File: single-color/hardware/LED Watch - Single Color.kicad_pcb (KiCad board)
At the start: 4 copper layers, 42 x 51.2 mm, 197 parts, among them J1 LiPo, J1B LiPo, J2 UPDI pogo pads 1.27 mm (RESET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, M0 LED white 0402, M1 LED white 0402, M10 LED white 0402, M11 LED white 0402, M12 LED white 0402, M13 LED white 0402, M14 LED white 0402, M15 LED white 0402, M16 LED white 0402, M17 LED white 0402, M18 LED white 0402, M19 LED white 0402, M2 LED white 0402, M20 LED white 0402, M21 LED white 0402, M22 LED white 0402, M23 LED white 0402, M24 LED white 0402, M25 LED white 0402, M26 LED white 0402, M27 LED white 0402, M28 LED white 0402, M29 LED white 0402, M3 LED white 0402, M30 LED white 0402, M31 LED white 0402, M32 LED white 0402, M33 LED white 0402, M34 LED white 0402, M35 LED white 0402, M36 LED white 0402, M37 LED white 0402, M38 LED white 0402, M39 LED white 0402, M4 LED white 0402, M40 LED white 0402, M41 LED white 0402, M42 LED white 0402, M43 LED white 0402, M44 LED white 0402, M45 LED white 0402, M46 LED white 0402, M47 LED white 0402, M48 LED white 0402, M49 LED white 0402, M5 LED white 0402, M50 LED white 0402, M51 LED white 0402, M52 LED white 0402, M53 LED white 0402, M54 LED white 0402, M55 LED white 0402, M56 LED white 0402, M57 LED white 0402, M58 LED white 0402, M59 LED white 0402, M6 LED white 0402, M7 LED white 0402, M8 LED white 0402, M9 LED white 0402, SW1 SW_Push, SW2 SW_Push, U1 AVR128DB48-I/6LX, U2 LIS2DW12TR, U4 BQ25570RGRR, Y1 32.768kHz

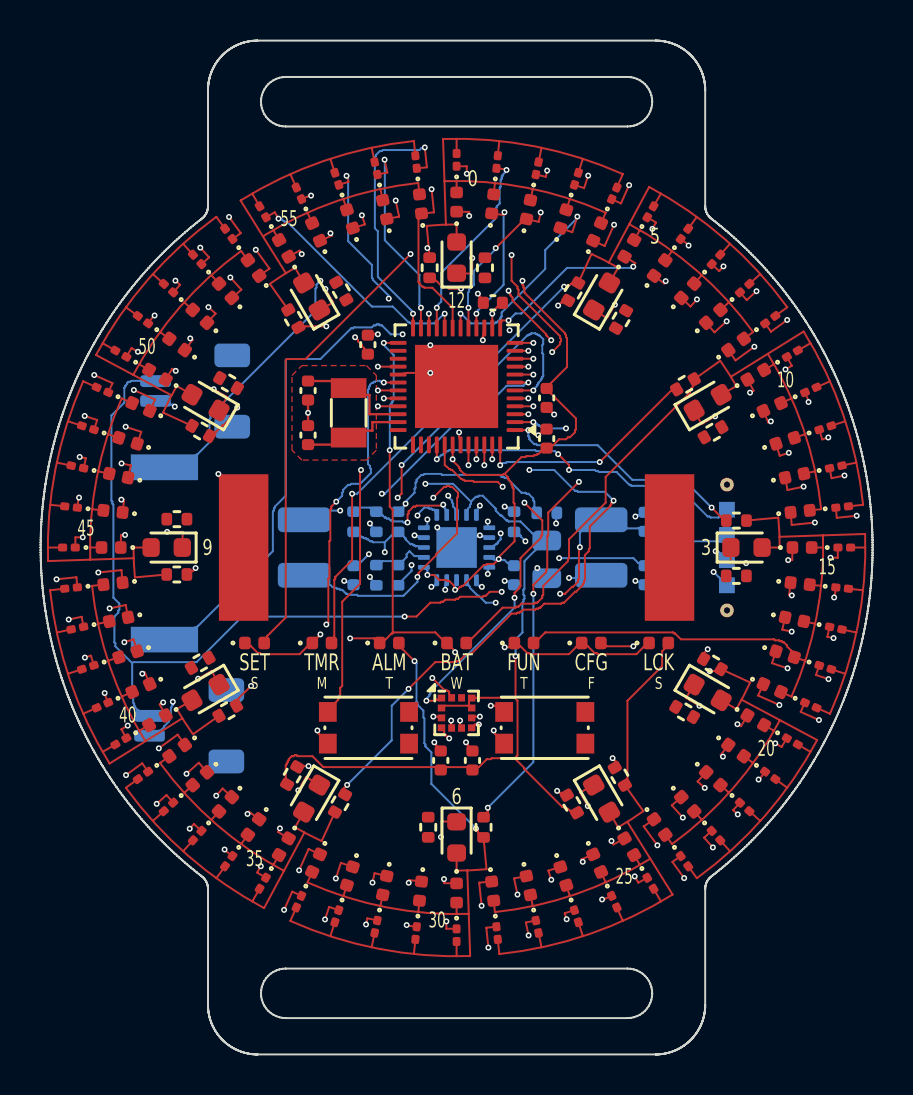
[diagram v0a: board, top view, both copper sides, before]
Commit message: single-color: re-route nets out from under the MCU (U1) and the harvester (U4); gerbers re-exported; tools for it; decision log
- BUZ_B off the In2 ground-plane layer; COL1, COL8_MCU, COL9_MCU, COL1_MCU, BUZ_B out of the MCU's 5x5 mm core; COL0_MCU partly (outside the centre); BTN2 and SDA out from under the BQ25570
- DRC 0 errors / 0 unconnected; BOM and placement files unchanged
- tools: reroute_prep.py, arcs_to_segments.py, prune_dangling_loop.py, prune_stub_vias.py

Co-Authored-By: Claude Sonnet 5.5 <noreply@anthropic.com>
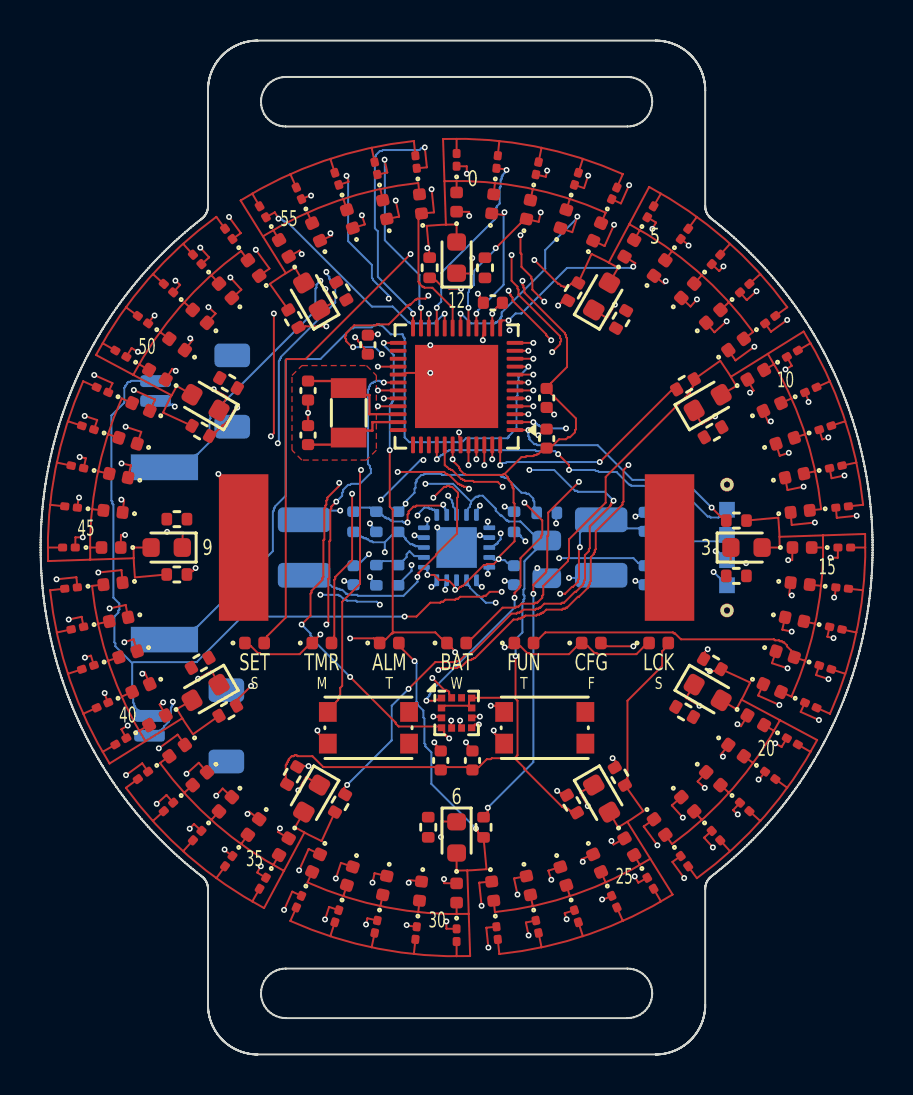
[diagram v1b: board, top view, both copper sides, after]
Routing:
- net /COL9_MCU: track 21.7 -> 39.1 mm, vias 3 -> 6
- net /COL8_MCU: track 29.4 -> 44.8 mm
- net /COL1: track 56.4 -> 70.4 mm, vias 2 -> 4
- net /COL0_MCU: track 14.7 -> 23.9 mm, vias 2 -> 5
- net /SDA: track 24.9 -> 34.2 mm, vias 3 -> 8
- net /BUZ_B: track 31.3 -> 38.8 mm, vias 2 -> 1
- net /COL1_MCU: track 10.4 -> 11.9 mm
- net /BTN2: track 25.2 -> 24.7 mm, vias 2 -> 6

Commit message: single-color: snap every track end to its via/pad centre (475 ends), zone refilled, gerbers re-exported; snap_centers.py; decision log
Co-Authored-By: Claude Sonnet 5.5 <noreply@anthropic.com>
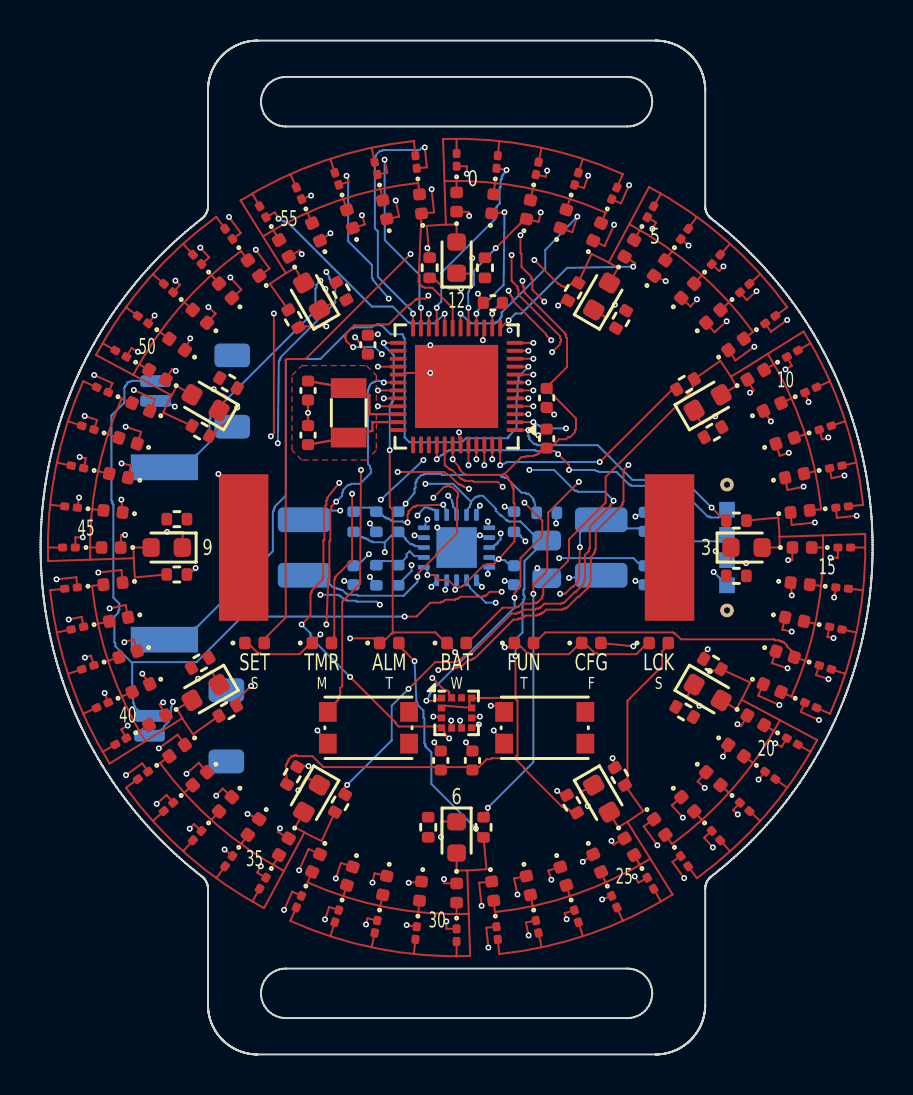
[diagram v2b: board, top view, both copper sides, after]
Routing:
- net GND: track 32.8 -> 28.8 mm
- net /ROW2: track 121.7 -> 118.8 mm
- net VBAT: track 54.6 -> 55.4 mm
- net /XTAL1: track 4.79 -> 5.61 mm
- net /XTAL2: track 4.25 -> 5.06 mm
- net /COL1_MCU: track 11.9 -> 12.6 mm
- net /BTN2: track 24.7 -> 25.3 mm
- net /VOUT_SET: track 6.62 -> 6.04 mm
- net /BUZ_B: track 38.8 -> 39.3 mm
- net /COL9_MCU: track 39.1 -> 39.6 mm

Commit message: single-color: reach of the centre snap fixed (via radius + half track width), grid wobble straightened (2091 -> 1468 pieces), gerbers re-exported
Co-Authored-By: Claude Sonnet 5.5 <noreply@anthropic.com>
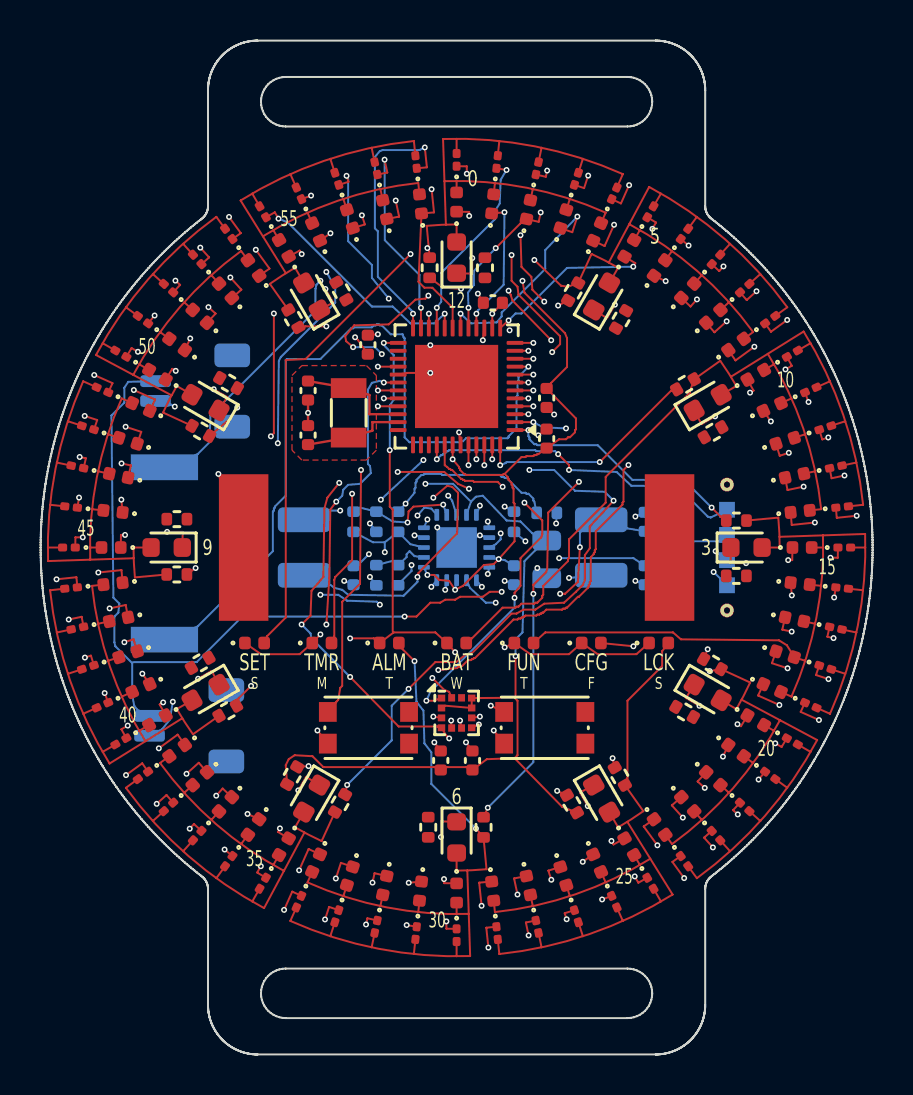
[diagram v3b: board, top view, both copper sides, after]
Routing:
- net /BTN1: track 18.3 -> 19.6 mm
- net GND: track 28.8 -> 27.6 mm
- net VBAT: track 55.4 -> 54.9 mm
- net /OK_PROG: track 11.3 -> 10.8 mm

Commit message: single-color: octilinear re-draw (non-45 pieces 790 -> 53), loose track joints welded to shared points, gerbers re-exported
Co-Authored-By: Claude Sonnet 5.5 <noreply@anthropic.com>
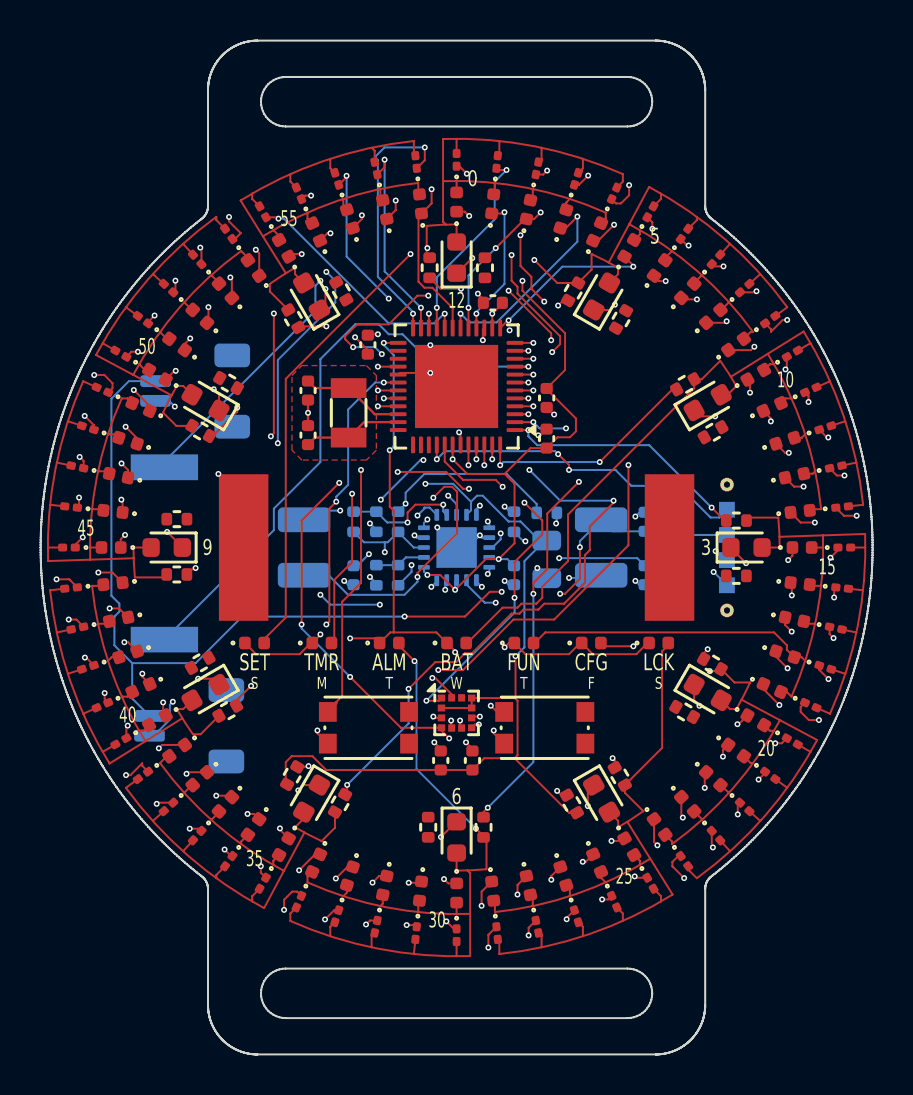
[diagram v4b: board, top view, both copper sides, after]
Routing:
- net /BUZ_B: track 39.3 -> 30.2 mm
- net /ROW0: track 113.3 -> 108.2 mm
- net /ROW5: track 139.5 -> 134.6 mm
- net /ROW4: track 136.2 -> 131.8 mm
- net /ROW9: track 145.3 -> 141.8 mm
- net /ROW3: track 126.9 -> 123.6 mm
- net /COL0_MCU: track 24.4 -> 21.7 mm
- net /ROW6: track 137.7 -> 135.2 mm
- net /VREF_SAMP: track 9.08 -> 6.67 mm
- net /ROW8: track 140.4 -> 138.1 mm
- net /ROW1: track 120.6 -> 119.1 mm
- net GND: track 27.6 -> 29.0 mm
- net /COL8_MCU: track 45.1 -> 44.2 mm
- net /COL5: track 40.6 -> 41.3 mm
- net +3V3: track 48.2 -> 48.9 mm
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
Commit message: single-color: pre-order review; VOUT divider R55/R56 to 7.32M/4.22M (inside the datasheet's recommended range), BOM 26 lines; review and no-oscilloscope bring-up test documents
Co-Authored-By: Claude Sonnet 5.5 <noreply@anthropic.com>
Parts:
- R55: value 6.49M -> 7.32M
- R56: value 3.74M -> 4.22M
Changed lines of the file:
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@@
 			)
 		)
-		(property "Value" "3.74M"
+		(property "Value" "4.22M"
 			(at 0 -1.17 90)
 			(layer "B.Fab")
@@
 			)
 		)
-		(property "Value" "6.49M"
+		(property "Value" "7.32M"
 			(at 0 -1.17 90)
 			(layer "B.Fab")

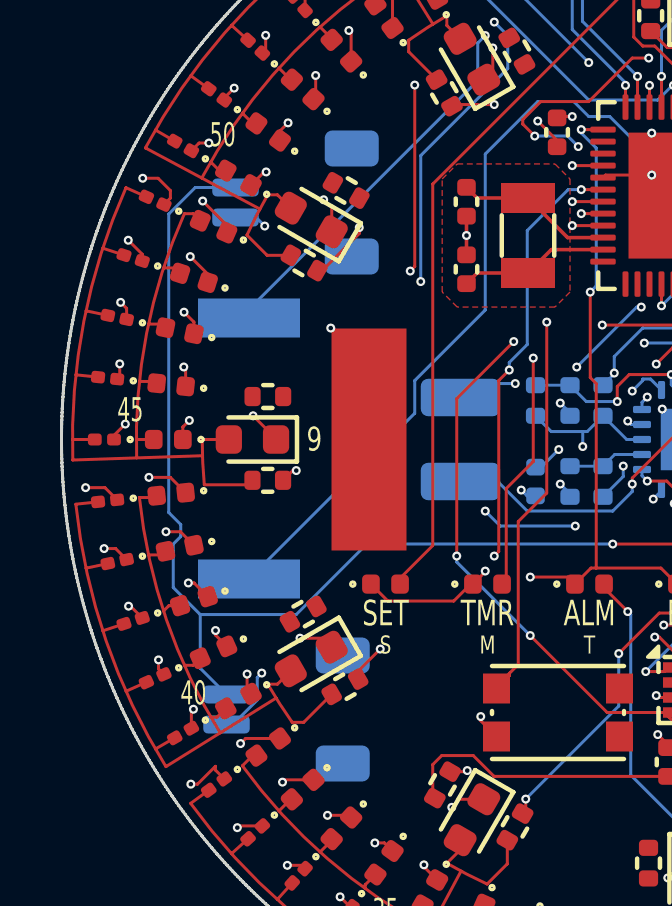
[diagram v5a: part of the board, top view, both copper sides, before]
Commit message: single-color: battery plug polarity swapped to match TinyCircuits' wiring (pin 1 = GND, pin 2 = BATT), local back rework + silk marks, schematic/netlist/gerbers/docs updated; review section 7
Co-Authored-By: Claude Sonnet 5.5 <noreply@anthropic.com>
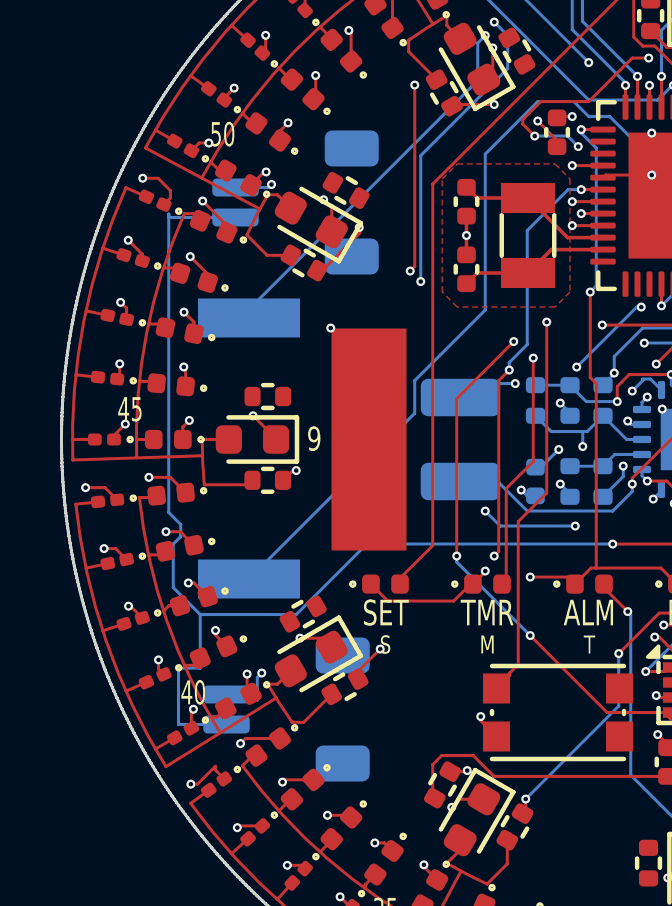
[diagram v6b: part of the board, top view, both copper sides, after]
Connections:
- J1 pad 1: /BATT -> GND
- J1 pad 2: GND -> /BATT
- J1B pad 1: /BATT -> GND
- J1B pad 2: GND -> /BATT
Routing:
- net /BATT: track 50.3 -> 53.0 mm
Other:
- board text added: "+"
- board text added: "-"
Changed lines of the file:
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@@
 			(layers "B.Cu" "B.Mask" "B.Paste")
 			(roundrect_rratio 0.25)
-			(net "/BATT")
+			(net "GND")
 		)
 		(pad "2" smd roundrect
@@
 			(layers "B.Cu" "B.Mask" "B.Paste")
 			(roundrect_rratio 0.25)
-			(net "GND")
+			(net "/BATT")
 		)
 		(pad "MP" smd roundrect
@@
 			(layers "B.Cu" "B.Mask" "B.Paste")
 			(roundrect_rratio 0.25)
-			(net "/BATT")
+			(net "GND")
 		)
 		(pad "2" smd roundrect
@@
 			(layers "B.Cu" "B.Mask" "B.Paste")
 			(roundrect_rratio 0.25)
-			(net "GND")
+			(net "/BATT")
 		)
 		(pad "MP" smd roundrect
@@
 		)
 	)
+	(gr_text "-"
+		(at 82.6 107.1 0)
+		(layer "B.SilkS")
+		(effects
+			(font
+				(size 1 1)
+				(thickness 0.15)
+			)
+			(justify mirror)
+		)
+	)
+	(gr_text "+"
+		(at 82.6 110.9 0)
+		(layer "B.SilkS")
+		(effects
+			(font
+				(size 1 1)
+				(thickness 0.15)
+			)
+			(justify mirror)
+		)
+	)
+	(gr_text "-"
+		(at 83.1 90.4 0)
+		(layer "B.SilkS")
+		(effects
+			(font
+				(size 1 1)
+				(thickness 0.15)
+			)
+			(justify mirror)
+		)
+	)
+	(gr_text "+"
+		(at 83.1 93.8 0)
+		(layer "B.SilkS")
+		(effects
+			(font
+				(size 1 1)
+				(thickness 0.15)
+			)
+			(justify mirror)
+		)
+	)
 	(gr_text "free centre 28.3 mm, LED band 7.59 mm, board 43.5 mm"
 		(at 100 72.25 0)
@@
 	)
 	(via
-		(at 85.775 92.885)
+		(at 86 91.5)
 		(size 0.3)
 		(drill 0.15)
@@
 	)
 	(segment
+		(start 84.8 91.6)
+		(end 85.9 91.6)
+		(width 0.1)
+		(layer "B.Cu")
+		(net "GND")
+	)
+	(segment
 		(start 85.525 107.935)
 		(end 85.675 107.785)
@@
 	)
 	(segment
+		(start 85.34 108.5)
+		(end 85.53 108.69)
+		(width 0.1)
+		(layer "B.Cu")
+		(net "GND")
+	)
+	(segment
 		(start 104.075 101.075)
 		(end 104.55 101.55)
@@
 	)
 	(segment
-		(start 85.49 92.6)
-		(end 84.8 92.6)
-		(width 0.1)
-		(layer "B.Cu")
-		(net "GND")
-	)
-	(segment
 		(start 101.29 99.5)
 		(end 101.65 99.5)
@@
 	)
 	(segment
-		(start 84.5 109.5)
-		(end 84.71 109.5)
-		(width 0.1)
-		(layer "B.Cu")
-		(net "GND")
-	)
-	(segment
 		(start 85.525 108.685)
 		(end 85.525 107.935)
@@
 	)
 	(segment
-		(start 85.775 92.885)
-		(end 85.49 92.6)
-		(width 0.1)
-		(layer "B.Cu")
-		(net "GND")
-	)
-	(segment
 		(start 101.275 101.985)
 		(end 101 101.71)
@@
 	)
 	(segment
-		(start 84.71 109.5)
-		(end 85.525 108.685)
-		(width 0.1)
-		(layer "B.Cu")
-		(net "GND")
-	)
-	(segment
 		(start 101.175 99.385)
 		(end 100.56 100)
@@
 	)
 	(segment
+		(start 85.9 91.6)
+		(end 86 91.5)
+		(width 0.1)
+		(layer "B.Cu")
+		(net "GND")
+	)
+	(segment
+		(start 84.5 108.5)
+		(end 85.34 108.5)
+		(width 0.1)
+		(layer "B.Cu")
+		(net "GND")
+	)
+	(segment
 		(start 115.870711 88.982266)
 		(end 115.870711 89.105825)
@@
 	)
 	(segment
-		(start 83.46 91.6)
-		(end 84.8 91.6)
-		(width 0.1)
-		(layer "B.Cu")
-		(net "/BATT")
-	)
-	(segment
-		(start 82.575 92.485)
-		(end 83.46 91.6)
+		(start 82.9 109.5)
+		(end 82.9 107.62)
 		(width 0.1)
 		(layer "B.Cu")
@@
 	)
 	(segment
+		(start 82.58 92.6)
+		(end 82.58 92.48)
+		(width 0.1)
+		(layer "B.Cu")
+		(net "/BATT")
+	)
+	(segment
 		(start 102.225 99.585)
 		(end 101.81 100)
@@
 	)
 	(segment
+		(start 82.9 107.62)
+		(end 83.62 107.62)
+		(width 0.1)
+		(layer "B.Cu")
+		(net "/BATT")
+	)
+	(segment
 		(start 82.575 102.435)
 		(end 82.575 92.485)
@@
 	)
 	(segment
+		(start 84.8 92.6)
+		(end 82.58 92.6)
+		(width 0.1)
+		(layer "B.Cu")
+		(net "/BATT")
+	)
+	(segment
 		(start 82.725 103.485)
 		(end 82.975 103.235)
@@
 	)
 	(segment
-		(start 83.625 107.625)
-		(end 84.5 108.5)
+		(start 84.5 109.5)
+		(end 82.9 109.5)
 		(width 0.1)
 		(layer "B.Cu")
